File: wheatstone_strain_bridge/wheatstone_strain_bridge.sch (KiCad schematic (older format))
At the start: 26 parts, among them J1 Conn_01x04, J10 Conn_01x10, J2 Conn_01x02, J3 Conn_01x04, J4 Conn_01x02, J5 Conn_01x04, J6 Conn_01x02, J7 Conn_01x04, J8 Conn_01x02, J9 Conn_01x10

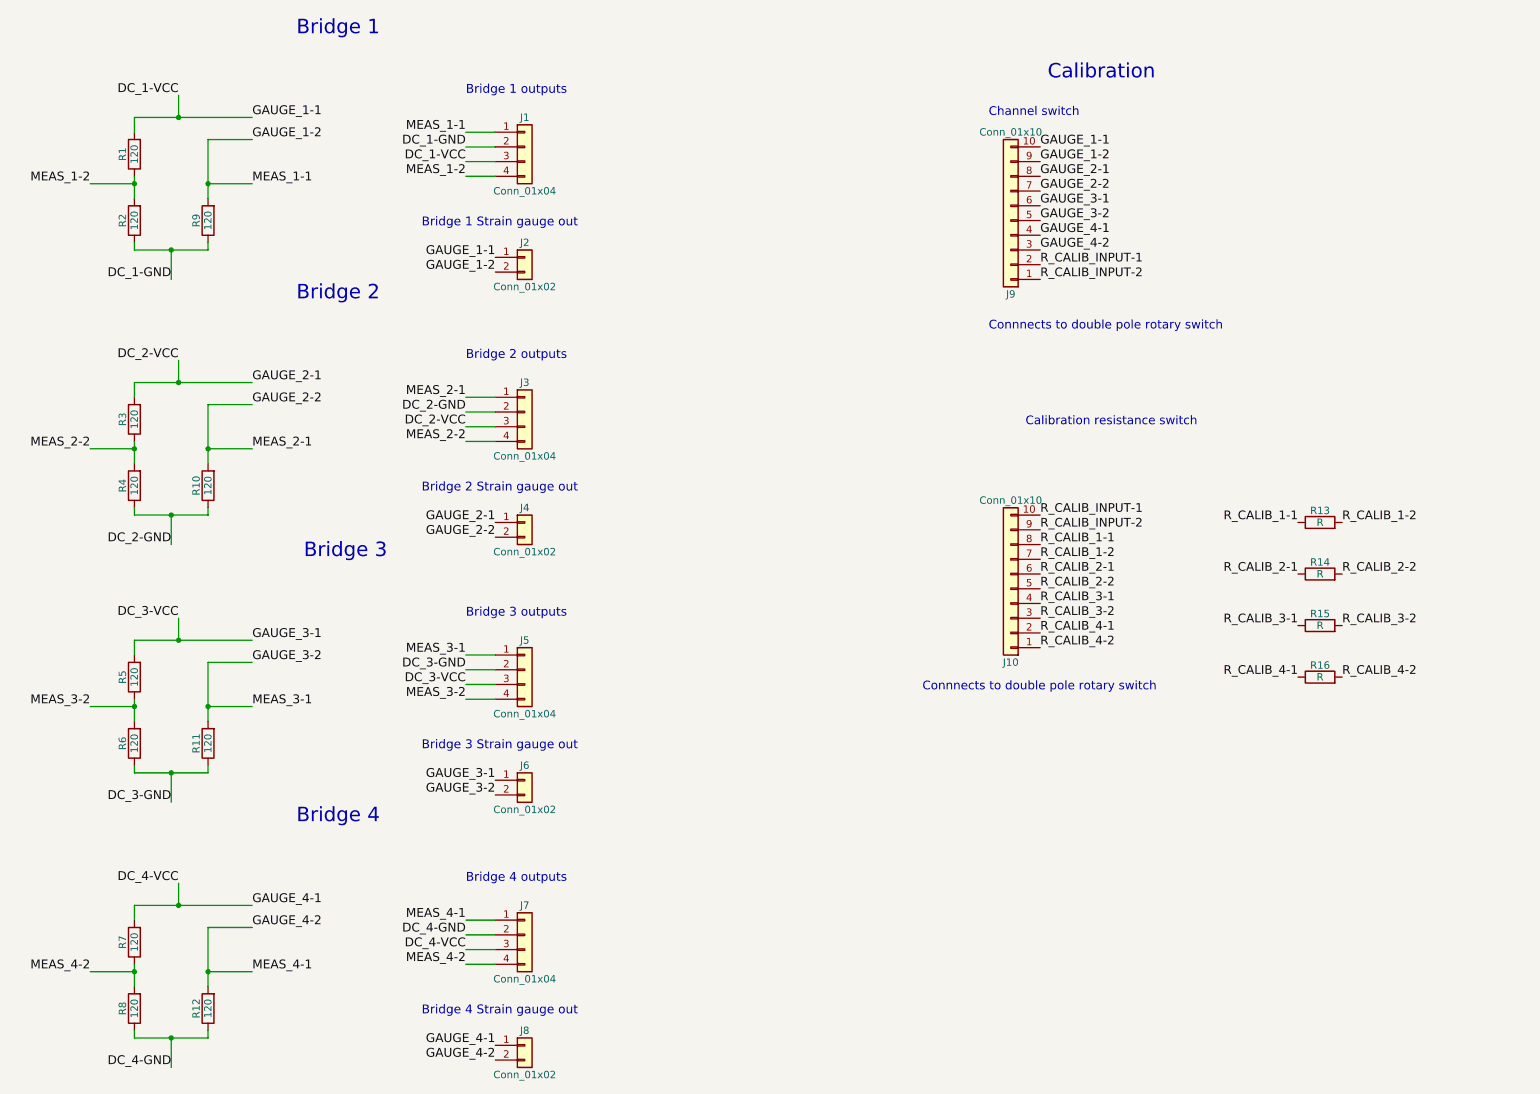
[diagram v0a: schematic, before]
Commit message: Working on new version with better jumper solution
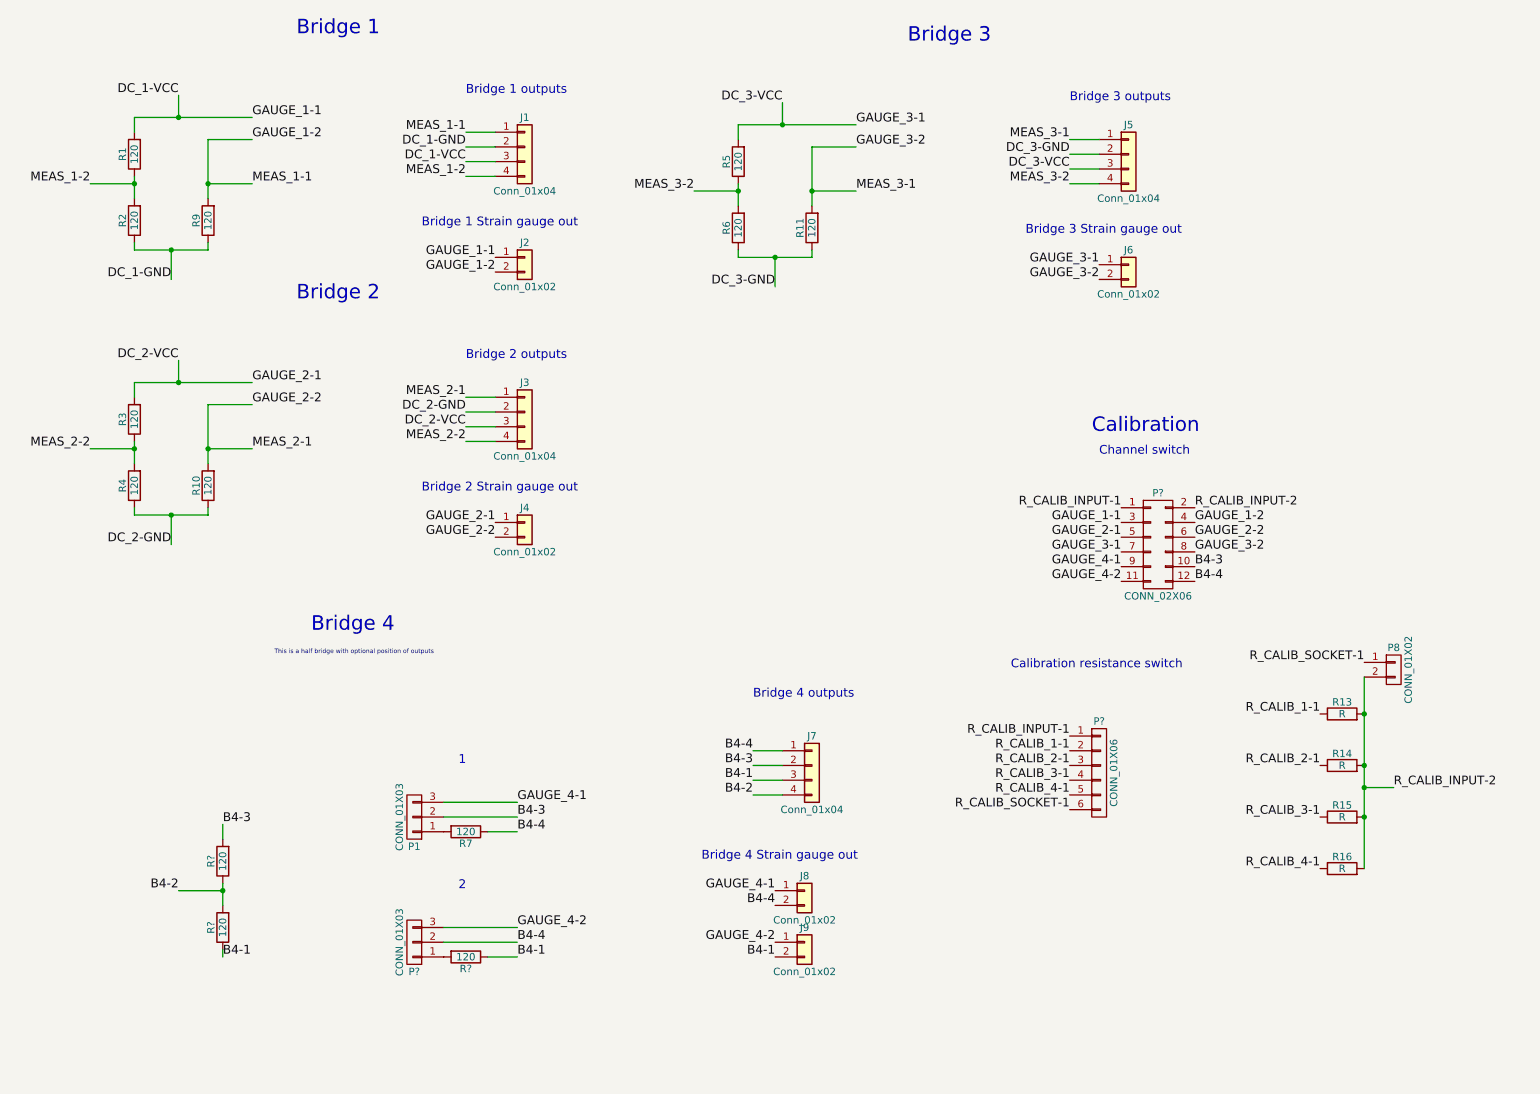
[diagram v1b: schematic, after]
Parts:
- removed J10, J9: Conn_01x10, Pin_Headers:Pin_Header_Straight_1x10_Pitch2.54mm, symbol Conn_01x10
- removed R12, R8: 120, Resistors_SMD:R_1210_HandSoldering, symbol R
- added J9: Conn_01x02, Pin_Headers:Pin_Header_Straight_1x02, symbol Conn_01x02
- added P1, P?: CONN_01X03, Pin_Headers:Pin_Header_Straight_1x03, symbol CONN_01X03
- added P8: CONN_01X02, Pin_Headers:Pin_Header_Straight_1x02, symbol CONN_01X02
- added P?: CONN_01X06, symbol CONN_01X06
- added P?: CONN_02X06, symbol CONN_02X06
- added R? (x3): 120, Resistors_SMD:R_1206_HandSoldering, symbol R
- J1, J3, J5, J7: footprint Pin_Headers:Pin_Header_Straight_1x04_Pitch2.54mm -> Pin_Headers:Pin_Header_Straight_1x04
- J2, J4, J6, J8: footprint Pin_Headers:Pin_Header_Straight_1x02_Pitch2.54mm -> Pin_Headers:Pin_Header_Straight_1x02
- R1, R10, R11, R13, R14, R15, R16, R2, R3, R4, R5, R6, R7, R9: footprint Resistors_SMD:R_1210_HandSoldering -> Resistors_SMD:R_1206_HandSoldering
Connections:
- net R_CALIB_1-2 is gone; now on net R_CALIB_INPUT-2: R13.2
- net R_CALIB_2-2 is gone; now on net R_CALIB_INPUT-2: R14.2
- net R_CALIB_3-2 is gone; now on net R_CALIB_INPUT-2: R15.2
- net R_CALIB_4-2 is gone; now on net R_CALIB_INPUT-2: R16.2
- net DC_1-VCC: now also P?.3 (P3)
- net DC_2-VCC: now also P?.5 (P5)
- net DC_3-VCC: now also P?.7 (P7)
- net GAUGE_1-2: now also P?.4 (P4)
- net GAUGE_2-2: now also P?.6 (P6)
- net GAUGE_3-2: now also P?.8 (P8)
- net GAUGE_4-2: now also J9.1 (Pin_1), P?.11 (P11), P?.3 (P3); no longer J7.1 (Pin_1), J8.2 (Pin_2)
- net R_CALIB_1-1: now also P?.2 (P2)
- net R_CALIB_2-1: now also P?.3 (P3)
- net R_CALIB_3-1: now also P?.4 (P4)
- net R_CALIB_4-1: now also P?.5 (P5)
- net R_CALIB_INPUT-1: now also P?.1 (P1), P?.1 (P1)
- net R_CALIB_INPUT-2: now also P8.2 (P2), P?.2 (P2)
- net DC_4-GND renamed B4-3
- net B4-3: now also P1.2 (P2), P?.10 (P10), R?.2
- removed net DC_4-VCC: J7.3 (Pin_3), J8.1 (Pin_1), R7.2
- net MEAS_4-2 renamed B4-2
- net B4-2: now also R?.1, R?.2; no longer R7.1
- new net: P1.1 (P1), R7.2
- new net: P?.1 (P1), R?.2
- new net B4-1: J7.3 (Pin_3), J9.2 (Pin_2), R?.1, R?.1
- new net B4-4: J7.1 (Pin_1), J8.2 (Pin_2), P?.12 (P12), P?.2 (P2), R7.1
- new net GAUGE_4-1: J8.1 (Pin_1), P1.3 (P3), P?.9 (P9)
- new net R_CALIB_SOCKET-1: P8.1 (P1), P?.6 (P6)
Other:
- note added: "1"
- note added: "2"
- note added: "This is a half bridge with optional position of outputs"
- note removed: "Connnects to double pole rotary switch"
- moved on the sheet: J5, J6, J7, J8, R11, R13, R14, R15, R16, R5, R6
